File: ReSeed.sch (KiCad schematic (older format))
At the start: 58 parts, among them CN1 EDGE_CONNECTOR, CN2 AUDIO_OUT, CN3 AUDIO_IN, CN4 DB9_MALE, Q1 BC549C, Q101 2SC1815, SW1 SW_DIGIFIX, U1 MOS_8580, U105 STEPUP_MT3608, U2 CD74HCT4520E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

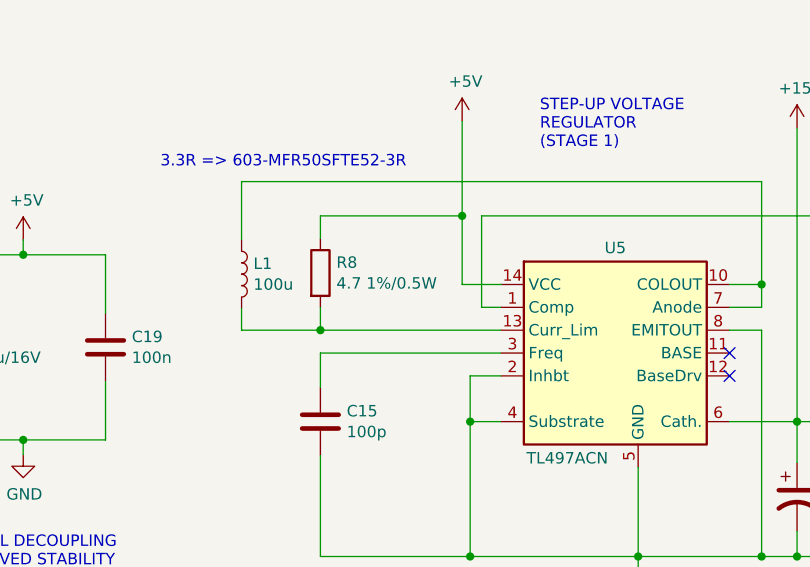
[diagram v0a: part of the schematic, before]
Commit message: R8 -> 3.3 ohm
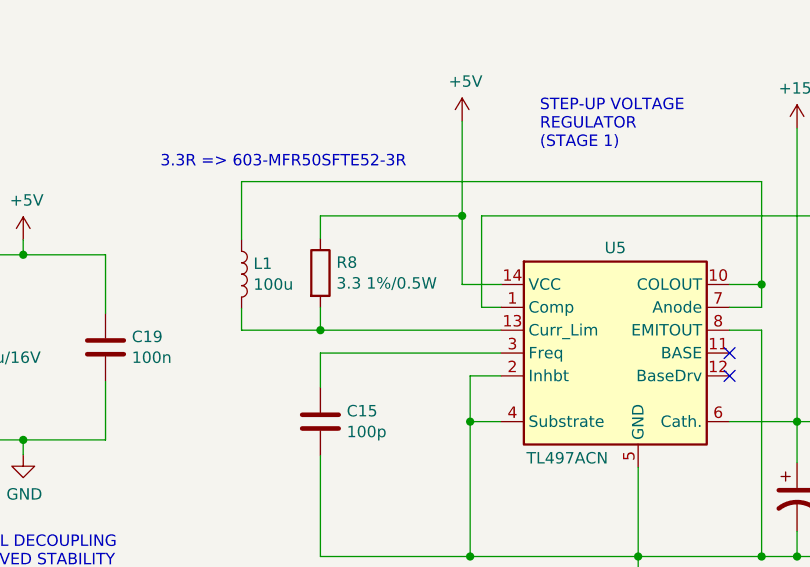
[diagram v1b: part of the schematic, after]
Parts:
- R8: value 4.7 1%/0.5W -> 3.3 1%/0.5W
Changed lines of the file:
@@
 Sheet 1 1
 Title "ReSeed"
-Date "2022-12-09"
+Date "2023-01-14"
 Rev "2git"
 Comp "SukkoPera/Kinmami"
@@
 P 6175 9335
 F 0 "R8" H 6245 9381 50  0000 L CNN
-F 1 "4.7 1%/0.5W" H 6245 9290 50  0000 L CNN
+F 1 "3.3 1%/0.5W" H 6245 9290 50  0000 L CNN
 F 2 "Resistor_THT:R_Axial_DIN0207_L6.3mm_D2.5mm_P10.16mm_Horizontal" V 6105 9335 50  0001 C CNN
 F 3 "~" H 6175 9335 50  0001 C CNN

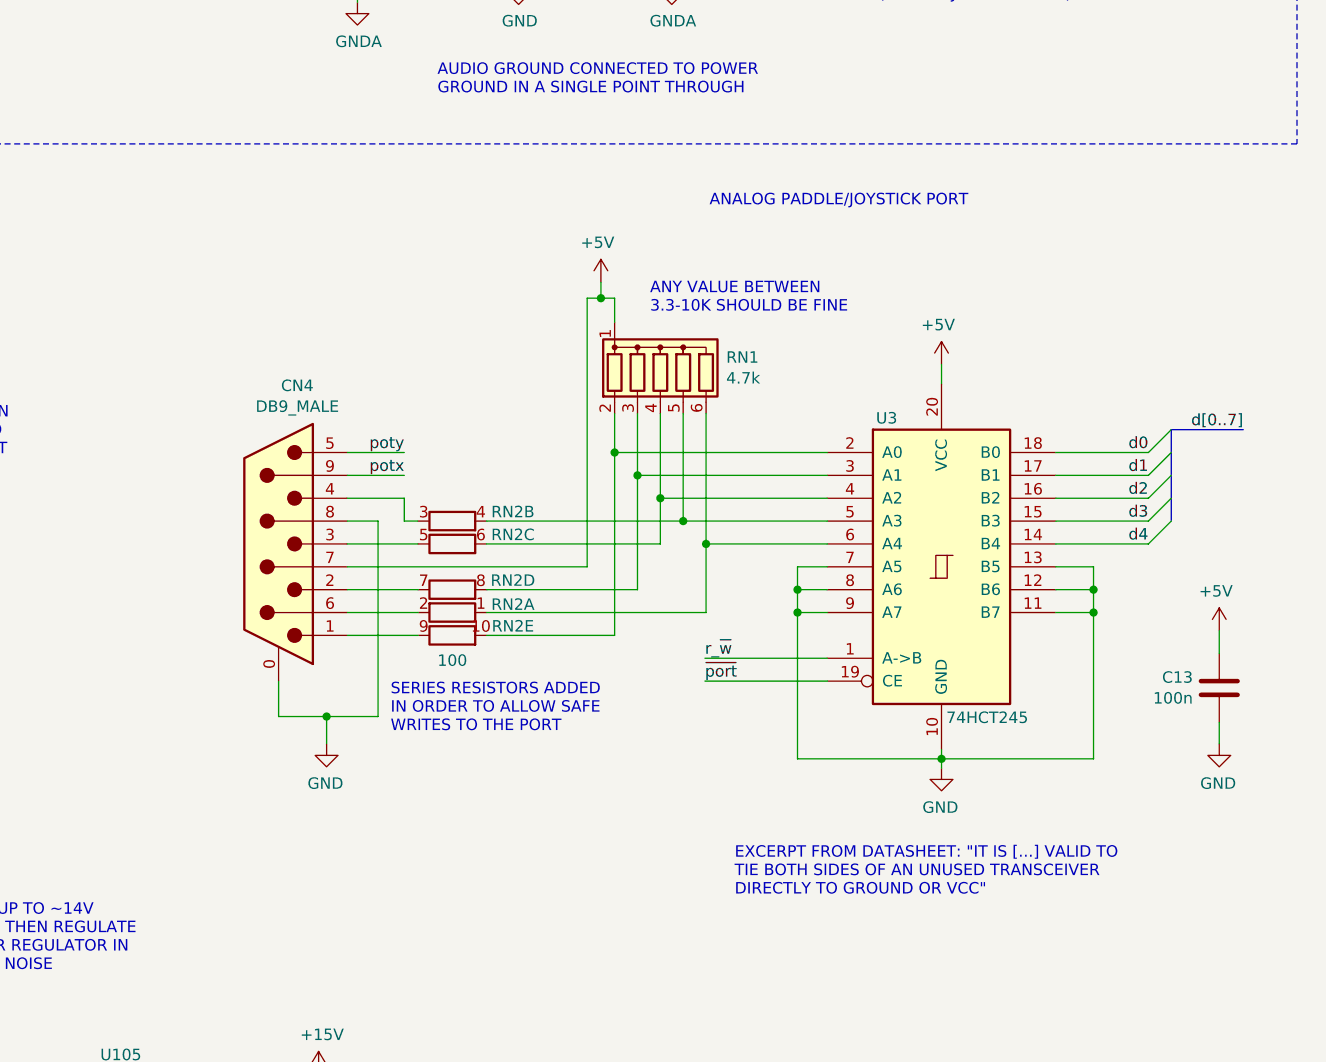
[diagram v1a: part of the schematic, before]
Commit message: Make D5-7 high on joystick reads Solder's joyport tester seems to require this, sigh...
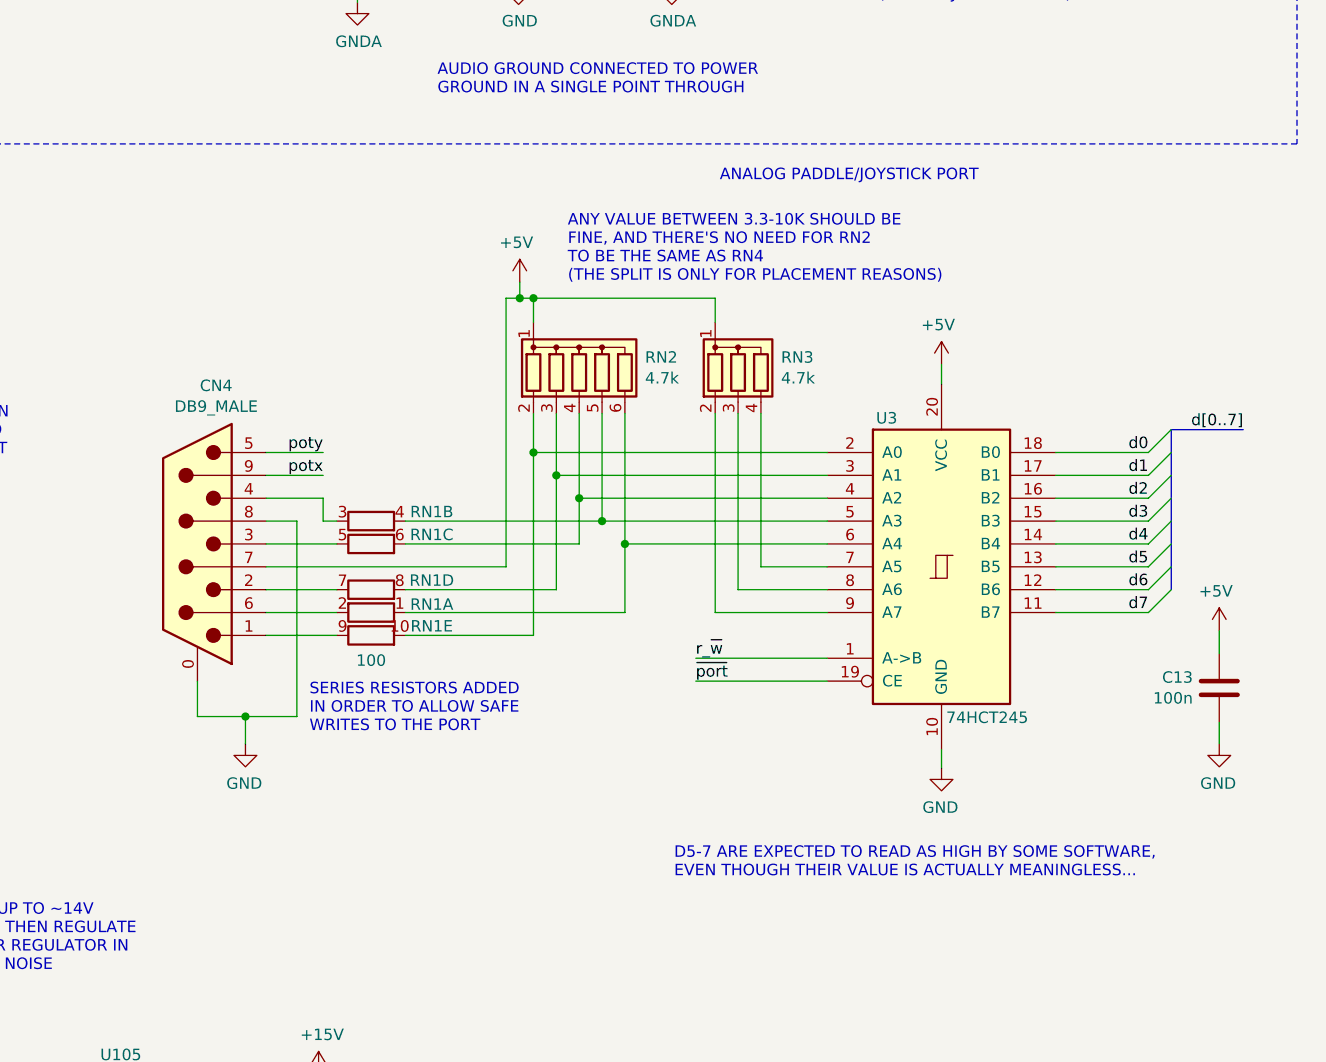
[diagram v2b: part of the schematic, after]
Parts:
- added RN3: 4.7k, Resistor_THT:R_Array_SIP4, symbol Device:R_Network03
- renumbered RN2 to RN1, RN1 to RN2
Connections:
- net +5V: now also RN3.1 (common)
- net GND: no longer U3.11 (B7), U3.12 (B6), U3.13 (B5), U3.7 (A5), U3.8 (A6), U3.9 (A7)
- net d5: now also U3.13 (B5)
- net d6: now also U3.12 (B6)
- net d7: now also U3.11 (B7)
- new net: RN3.4 (R3), U3.7 (A5)
- new net: RN3.3 (R2), U3.8 (A6)
- new net: RN3.2 (R1), U3.9 (A7)
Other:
- note added: "ANY VALUE BETWEEN 3.3-10K SHOULD BE\nFINE, AND THERE'S NO NEED FOR RN2\nTO BE THE SAME AS RN4\n(THE SPLIT IS ONLY FOR PLACEMENT REASONS)"
- note added: "D5-7 ARE EXPECTED TO READ AS HIGH BY SOME SOFTWARE,\nEVEN THOUGH THEIR VALUE IS ACTUALLY MEANINGLESS..."
- note removed: "ANY VALUE BETWEEN\n3.3-10K SHOULD BE FINE"
- note removed: "EXCERPT FROM DATASHEET: "IT IS [...] VALID TO\nTIE BOTH SIDES OF AN UNUSED TRANSCEIVER\nDIRECTLY TO GROUND OR VCC""
- moved on the sheet: CN4, RN1A, RN1B, RN1C, RN1D, RN1E, RN2

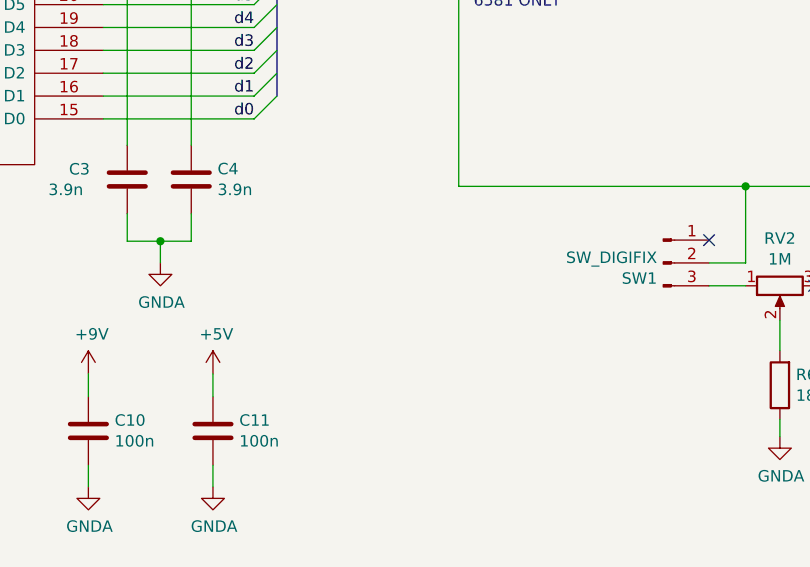
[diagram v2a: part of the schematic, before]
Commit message: Add note on C3/4
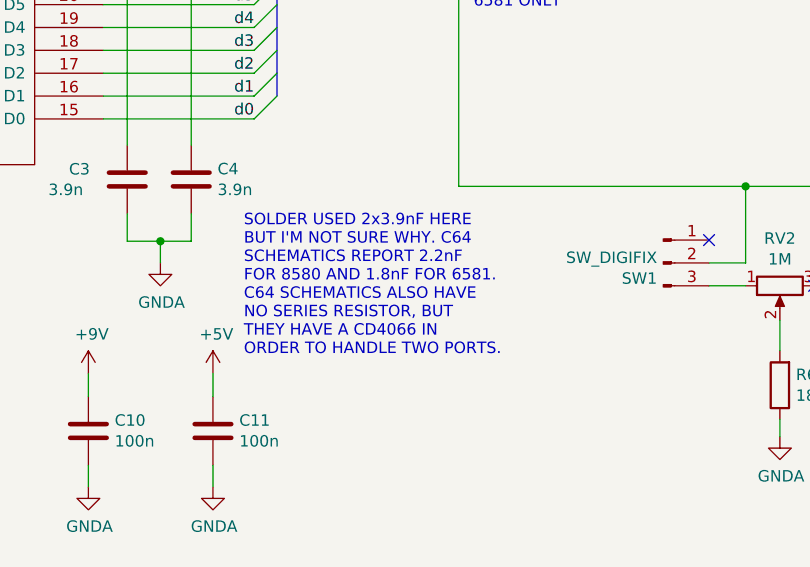
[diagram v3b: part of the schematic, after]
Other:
- note added: "SOLDER USED 2x3.9nF HERE\nBUT I'M NOT SURE WHY. C64\nSCHEMATICS REPORT 2.2nF\nFOR 8580 AND 1.8nF FOR 6581.\nC64 SCHEMATICS ALSO HAVE\nNO SERIES RESISTOR, BUT\nTHEY HAVE A CD4066 IN\nORDER TO HANDLE TWO PORTS."
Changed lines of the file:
@@
 Wire Bus Line
 	6450 5890 6450 6845
+Text Notes 9475 3935 0    50   ~ 0
+SOLDER USED 2x3.9nF HERE\nBUT I'M NOT SURE WHY. C64\nSCHEMATICS REPORT 2.2nF\nFOR 8580 AND 1.8nF FOR 6581.\nC64 SCHEMATICS ALSO HAVE\nNO SERIES RESISTOR, BUT\nTHEY HAVE A CD4066 IN\nORDER TO HANDLE TWO PORTS.
 $EndSCHEMATC

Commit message: Add P/N for Q101
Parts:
- Q1: Notes (none) -> Either mount this or Q101
- Q101: MouserPN (none) -> 610-2SC1815-GR; Notes (none) -> Either mount this or Q1
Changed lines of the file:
@@
 F 3 "https://www.onsemi.com/pub/Collateral/BC550-D.pdf" H 12730 1495 50  0001 L CNN
 F 4 "512-BC549CTA" H 12730 1495 50  0001 C CNN "MouserPN"
+F 5 "Either mount this or Q101" H 12730 1495 50  0001 C CNN "Notes"
 	1    12730 1495
 	1    0    0    -1
@@
 F 2 "Package_TO_SOT_THT:TO-92_HandSolder" H 12565 1165 50  0001 L CIN
 F 3 "https://media.digikey.com/pdf/Data%20Sheets/Toshiba%20PDFs/2SC1815.pdf" H 12365 1240 50  0001 L CNN
+F 4 "610-2SC1815-GR" H 12365 1240 50  0001 C CNN "MouserPN"
+F 5 "Either mount this or Q1" H 12365 1240 50  0001 C CNN "Notes"
 	1    12365 1240
 	1    0    0    -1
@@
 Wire Wire Line
 	14875 6755 15280 6755
+Text Notes 9475 3935 0    50   ~ 0
+SOLDER USED 2x3.9nF HERE\nBUT I'M NOT SURE WHY. C64\nSCHEMATICS REPORT 2.2nF\nFOR 8580 AND 1.8nF FOR 6581.\nC64 SCHEMATICS ALSO HAVE\nNO SERIES RESISTOR, BUT\nTHEY HAVE A CD4066 IN\nORDER TO HANDLE TWO PORTS.
 Wire Bus Line
 	8650 5890 8650 6745
@@
 Wire Bus Line
 	6450 5890 6450 6845
-Text Notes 9475 3935 0    50   ~ 0
-SOLDER USED 2x3.9nF HERE\nBUT I'M NOT SURE WHY. C64\nSCHEMATICS REPORT 2.2nF\nFOR 8580 AND 1.8nF FOR 6581.\nC64 SCHEMATICS ALSO HAVE\nNO SERIES RESISTOR, BUT\nTHEY HAVE A CD4066 IN\nORDER TO HANDLE TWO PORTS.
 $EndSCHEMATC

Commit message: Make C3/4 SID-model-dependent
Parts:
- C1, C2: Notes (none) -> For 6581 use 470pF; Value (none) -> 22n
- C10, C11, C12, C13, C14, C17, C19, C7, C9: Value (none) -> 100n
- C15: Value (none) -> 100p
- C16: Value (none) -> 1000u/25V
- C18: Value (none) -> 100u/16V
- C20: Notes (none) -> If using old CD4520 as U2 do not mount C20; Value (none) -> 470p
- C21, C8: Value (none) -> 10u
- C3, C4: value 3.9n -> 2.2n; MouserPN 810-FG28C0G1H392JNT6 -> 810-FG28C0G1H222JNT6; Notes (none) -> For 6581 use 1.8nF; Value (none) -> 2.2n
- C5: Value (none) -> 1n
- C6: Value (none) -> 470p
- CN1: Value (none) -> EDGE_CONNECTOR
- CN2: Value (none) -> AUDIO_OUT
- CN3: Value (none) -> AUDIO_IN
- CN4: Value (none) -> DB9_MALE
- FB1, FB2: Value (none) -> 28C0236-0EW-10
- JP1: Value (none) -> JMP_GND_LIFT
- JP2: Value (none) -> JMP_CNT_RST
- JP3: Value (none) -> JMP_REG_BYPASS
- L1: Value (none) -> 100u
- Q1: Value (none) -> BC549C
- Q101: Value (none) -> 2SC1815
- R1, R2, RN1: Value (none) -> 100
- R10: Value (none) -> 1.2k 1%
- R11: Notes (none) -> If using old CD4520 as U2 replace R11 with 0R; Value (none) -> 100
- R3: Notes (none) -> For 6581 do not mount R3; Value (none) -> 1k
- R4, RV1: Value (none) -> 10k
- R5: Value (none) -> 1k
- R6: Notes (none) -> For 6581 do not mount; Value (none) -> 180k
- R7: Value (none) -> 100k
- R8: MouserPN 603-MFR50SFTE52-4R7 -> 603-MFR50SFTE52-3R3; Value (none) -> 3.3 1%/0.5W
- R9: MouserPN 71-CMF557K8700FHEK -> 603-MFR-25FRF52-12K7; Notes (none) -> If U6 is not mounted use (IMPORTANT!) 11k for 6581 or (IMPO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; Value (none) -> 12.7k 1%
- RN2, RN3: Value (none) -> 4.7k
- RV2: Notes (none) -> For 6581 do not mount; Value (none) -> 1M
- SW1: Notes (none) -> For 6581 do not mount; Value (none) -> SW_DIGIFIX
- U1: Value (none) -> MOS_8580
- U105: Notes (none) -> If willing to use this, check wiki (Actually check it ANYWA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; Value (none) -> STEPUP_MT3608
- U2: Notes (none) -> Use old CD4520B if possible; Value (none) -> CD74HCT4520E
- U3: Value (none) -> 74HCT245
- U4: Value (none) -> GAL16V8
- U5: Value (none) -> TL497ACN
- U6: value L7809 -> LM7809; Notes (none) -> For 6581 use LM7812, if not mounted short JP3 and (IMPORTAN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; Value (none) -> LM7809
- V0: Value (none) -> LOGO
- V1: Value (none) -> LICENSE
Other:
- note added: "R1/2 APPROXIMATE THE ON-RESISTANCE\nOF THE CD4066 USED IN THE ORIGINAL\nC64 CIRCUIT IN ORDER TO HANDLE TWO PORTS"
- note added: "SOLDER USED 2x3.9nF HERE\nBUT I'M NOT SURE WHY. C64\nUSES 2.2nF FOR 8580 AND\n1.8nF FOR 6581, WHICH SEEM\nTO ALLOW FOR AN EXTENDED\nANALOG RANGE IN MY EXPERIENCE"
- note removed: "SOLDER USED 2x3.9nF HERE\nBUT I'M NOT SURE WHY. C64\nSCHEMATICS REPORT 2.2nF\nFOR 8580 AND 1.8nF FOR 6581.\nC64 SCHEMATICS ALSO HAVE\nNO SERIES RESISTOR, BUT\nTHEY HAVE A CD4066 IN\nORDER TO HANDLE TWO PORTS."

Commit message: BOM fixes for #1 and README update
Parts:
- C15: MouserPN 80-C327C131JAG5TA -> 810-FG28C0G1H101JNT6
- Q1: Notes Either mount this or Q101 -> Either mount this or Q101, BC547 and BC548 would work but B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
- RN2: Notes (none) -> Any value between 3.3-10K should be fine
- RN3: value 4.7k -> 10k; MouserPN 652-4604X-1LF-4.7K -> 652-4604X-1LF-10K
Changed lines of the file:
@@
 F 2 "Capacitor_THT:C_Disc_D7.0mm_W2.5mm_P5.00mm" H 6213 9835 50  0001 C CNN
 F 3 "~" H 6175 9985 50  0001 C CNN
-F 4 "80-C327C131JAG5TA" H 6175 9985 50  0001 C CNN "MouserPN"
+F 4 "810-FG28C0G1H101JNT6" H 6175 9985 50  0001 C CNN "MouserPN"
 F 5 "100p" H 6175 9985 50  0001 C CNN "Value"
 	1    6175 9985
@@
 F 3 "https://www.onsemi.com/pub/Collateral/BC550-D.pdf" H 12730 1495 50  0001 L CNN
 F 4 "512-BC549CTA" H 12730 1495 50  0001 C CNN "MouserPN"
-F 5 "Either mount this or Q101" H 12730 1495 50  0001 C CNN "Notes"
+F 5 "Either mount this or Q101, BC547 and BC548 would work but BC549 is low-noise" H 12730 1495 50  0001 C CNN "Notes"
 F 6 "BC549C" H 12730 1495 50  0001 C CNN "Value"
 	1    12730 1495
@@
 F 4 "652-4606X-1LF-4.7K" H 12790 5885 50  0001 C CNN "MouserPN"
 F 5 "4.7k" H 12790 5885 50  0001 C CNN "Value"
+F 6 "Any value between 3.3-10K should be fine" H 12790 5885 50  0001 C CNN "Notes"
 	1    12790 5885
 	1    0    0    -1
@@
 P 13485 5885
 F 0 "RN3" H 13673 5931 50  0000 L CNN
-F 1 "4.7k" H 13673 5840 50  0000 L CNN
+F 1 "10k" H 13673 5840 50  0000 L CNN
 F 2 "Resistor_THT:R_Array_SIP4" V 13760 5885 50  0001 C CNN
 F 3 "http://www.vishay.com/docs/31509/csc.pdf" H 13485 5885 50  0001 C CNN
-F 4 "652-4604X-1LF-4.7K" H 13485 5885 50  0001 C CNN "MouserPN"
+F 4 "652-4604X-1LF-10K" H 13485 5885 50  0001 C CNN "MouserPN"
 F 5 "4.7k" H 13485 5885 50  0001 C CNN "Value"
 	1    13485 5885

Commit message: Fix confusion about R3 - See #3
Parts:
- R3: Notes For 6581 do not mount R3 -> For 8580 do not mount R3
- R5: Notes (none) -> For 8580 do not mount R3
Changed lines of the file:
@@
 F 4 "603-MFR-25FBF52-1K" H 12830 2080 50  0001 C CNN "MouserPN"
 F 5 "1k" H 12830 2080 50  0001 C CNN "Value"
+F 6 "For 8580 do not mount R3" H 12830 2080 50  0001 C CNN "Notes"
 	1    12830 2080
 	-1   0    0    1
@@
 F 3 "~" H 10720 1775 50  0001 C CNN
 F 4 "603-MFR-25FBF52-1K" H 10720 1775 50  0001 C CNN "MouserPN"
-F 5 "For 6581 do not mount R3" H 10720 1775 50  0001 C CNN "Notes"
+F 5 "For 8580 do not mount R3" H 10720 1775 50  0001 C CNN "Notes"
 F 6 "1k" H 10720 1775 50  0001 C CNN "Value"
 	1    10720 1775
